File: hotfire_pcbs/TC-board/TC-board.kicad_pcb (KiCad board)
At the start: 2 copper layers, 20.3 x 8.4 mm, 14 parts, among them J1 JST, J2 JST, J3 PCIE-LP-01-01-F-DV-A-TR, U1 MAX31856_Breakout, U2 MAX31856_Breakout

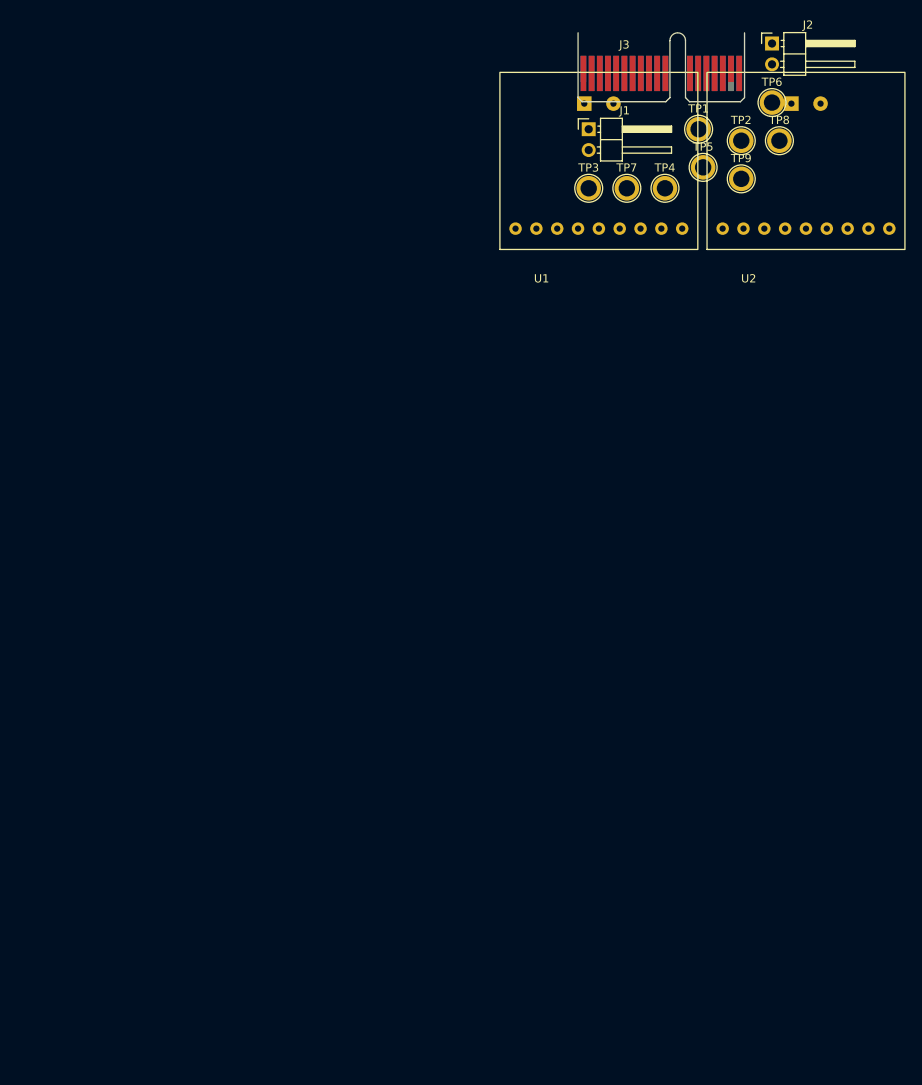
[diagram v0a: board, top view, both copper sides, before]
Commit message: TC Board Layout
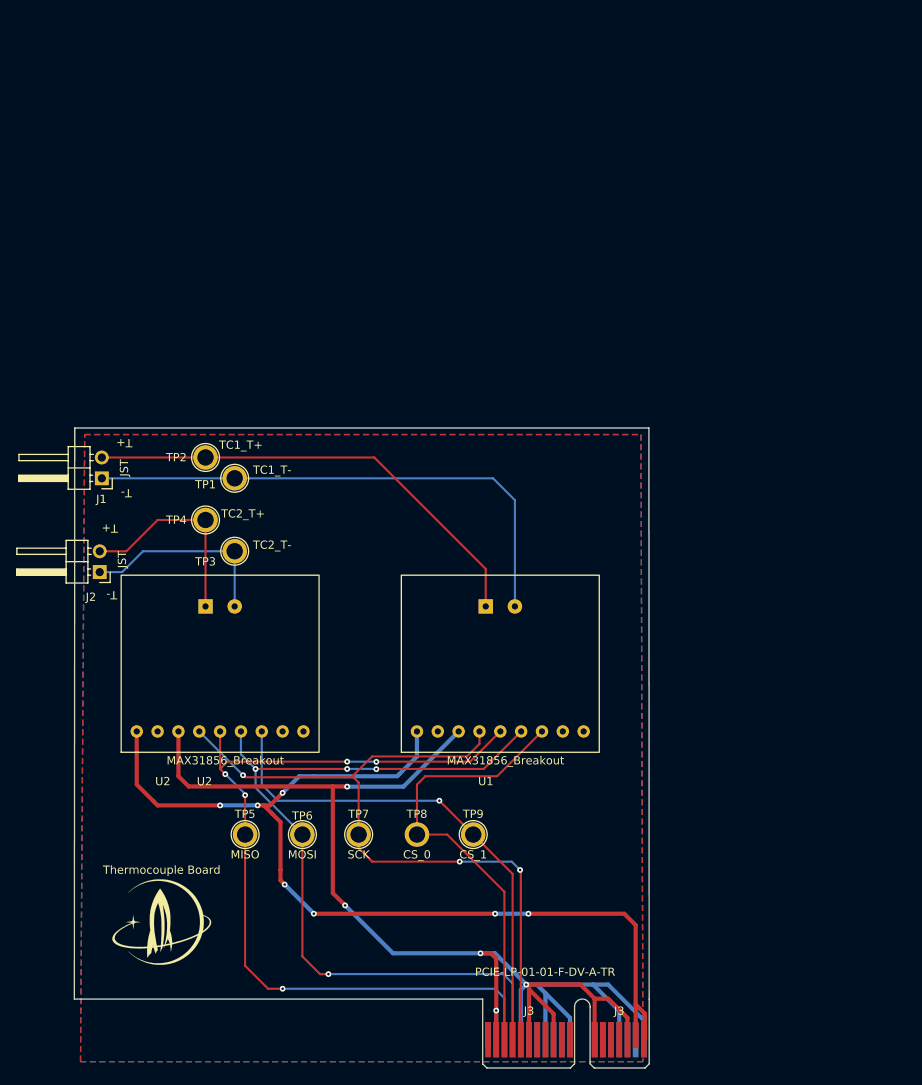
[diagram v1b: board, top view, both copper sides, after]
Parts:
- added G***: LOGO, star-common-lib:star_12x10, F.Cu at (175.8, 120.1)
- added G***: LOGO, LOGO, B.Cu at (227.1, 69.8)
- TP1: value TestPoint -> TC1_T-
- TP2: value TestPoint -> TC1_T+
- TP3: value TestPoint -> TC2_T-
- TP4: value TestPoint -> TC2_T+
- TP5: value TestPoint -> MISO
- TP6: value TestPoint -> MOSI
- TP7: value TestPoint -> SCK
- TP8: value TestPoint -> CS_0; moved to B.Cu
- TP9: value TestPoint -> CS_1
- moved J3 118.4 mm to (215.5, 134.5)
- moved TP6 106.0 mm to (192.9, 109.5)
- moved J2 104.3 mm to (168.2, 77.5), turned to 180 degrees
- moved TP5 98.7 mm to (185.9, 109.5)
- moved TP8 95.4 mm to (206.9, 109.5), turned to 180 degrees
- moved U2 94.1 mm to (183.5, 85.2)
- moved TP9 86.4 mm to (213.7, 109.5)
- moved TP7 85.3 mm to (199.8, 109.5)
- moved TP2 75.9 mm to (181.1, 63.5), turned to 90 degrees
- moved J1 73.0 mm to (168.5, 66.0), turned to 180 degrees
- moved TP1 70.8 mm to (184.7, 66.0), turned to 90 degrees
- moved TP4 69.1 mm to (181.1, 71.1), turned to 90 degrees
- moved U1 62.5 mm to (217.7, 85.2)
- moved TP3 61.8 mm to (184.7, 74.9), turned to 90 degrees
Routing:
- net GND: track 0.00 -> 183.3 mm, vias 0 -> 5
- net +3V3: track 0.00 -> 121.0 mm, vias 0 -> 7
- net /SPI_MISO: track 0.00 -> 104.1 mm, vias 0 -> 5
- net /SPI_MOSI: track 0.00 -> 98.7 mm, vias 0 -> 4
- net /SPI_SCK: track 0.00 -> 90.2 mm, vias 0 -> 3
- net /TC1_T-: track 0.00 -> 64.4 mm
- net /SPI_CS_1: track 0.00 -> 61.8 mm, vias 0 -> 1
- net /TC1_T+: track 0.00 -> 57.0 mm
- net /SPI_CS_0: track 0.00 -> 55.6 mm
- net /TC2_T+: track 0.00 -> 25.0 mm
- net /TC2_T-: track 0.00 -> 24.2 mm
- added copper zone on B.Cu, net GND
- added copper zone on F.Cu, net GND
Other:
- board size 20.3 x 8.4 mm -> 70.1 x 69.6 mm
- board text added: "T+"
- board text added: "T-"
- board text added: "Thermocouple Board"

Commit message: Changed JST to DSUB
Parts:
- removed J2: JST, Connector_PinHeader_2.54mm:PinHeader_1x02_P2.54mm_Horizontal
- J1: value JST -> DB15_Female; footprint Connector_PinHeader_2.54mm:PinHeader_1x02_P2.54mm_Horizontal -> DSUB_622-015-260-042:DSUB_622-015-260-042
- TP1: value TC1_T- -> TestPoint; footprint TestPoint:TestPoint_Plated_Hole_D2.0mm -> TestPoint:TestPoint_Keystone_5010-5014_Multipurpose
- TP2: value TC1_T+ -> TestPoint; footprint TestPoint:TestPoint_Plated_Hole_D2.0mm -> TestPoint:TestPoint_Keystone_5010-5014_Multipurpose
- TP3: value TC2_T- -> TestPoint; footprint TestPoint:TestPoint_Plated_Hole_D2.0mm -> TestPoint:TestPoint_Keystone_5010-5014_Multipurpose
- TP4: value TC2_T+ -> TestPoint; footprint TestPoint:TestPoint_Plated_Hole_D2.0mm -> TestPoint:TestPoint_Keystone_5010-5014_Multipurpose
- TP5: value MISO -> TestPoint; footprint TestPoint:TestPoint_Plated_Hole_D2.0mm -> TestPoint:TestPoint_Keystone_5010-5014_Multipurpose
- TP6: value MOSI -> TestPoint; footprint TestPoint:TestPoint_Plated_Hole_D2.0mm -> TestPoint:TestPoint_Keystone_5010-5014_Multipurpose
- TP7: value SCK -> TestPoint; footprint TestPoint:TestPoint_Plated_Hole_D2.0mm -> TestPoint:TestPoint_Keystone_5010-5014_Multipurpose
- TP8: value CS_0 -> TestPoint; footprint TestPoint:TestPoint_Plated_Hole_D2.0mm -> TestPoint:TestPoint_Keystone_5010-5014_Multipurpose
- TP9: value CS_1 -> TestPoint; footprint TestPoint:TestPoint_Plated_Hole_D2.0mm -> TestPoint:TestPoint_Keystone_5010-5014_Multipurpose
- moved J1 26.7 mm to (176.5, 91.5), turned to -90 degrees
- moved G*** 0.96 mm to (175.8, 121.1)
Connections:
- J1 pad 2: /TC1_T+ -> /TC2_T-
- J3 pad B17: +3V3 -> (no net)
- J3 pad B18: +3V3 -> (no net)
- U1 pad 11: +3V3 -> +3.3V
- U2 pad 11: +3V3 -> +3.3V
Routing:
- net +3V3: track 121.0 -> 0.00 mm, vias 7 -> 0
- net +3.3V: track 0.00 -> 121.0 mm, vias 0 -> 7
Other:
- board text removed: "T+"
- board text removed: "T-"

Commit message: Updated TC Board
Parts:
- TP1: value TestPoint -> TC1_T-
- TP2: value TestPoint -> TC1_T+
- TP3: value TestPoint -> TC2_T-
- TP4: value TestPoint -> TC2_T+
- TP5: value TestPoint -> MISO
- TP6: value TestPoint -> MOSI
- TP7: value TestPoint -> SCK
- TP8: value TestPoint -> CS_0
- TP9: value TestPoint -> CS_1
- moved TP1 39.9 mm to (222.2, 79.5), turned to 0 degrees
- moved TP2 39.1 mm to (216.8, 79.4), turned to 0 degrees
- moved TP5 21.0 mm to (203.3, 121.2)
- moved TP6 21.0 mm to (210.3, 121.2)
- moved TP7 21.0 mm to (217.2, 121.2)
- moved TP8 21.0 mm to (224.3, 121.2)
- moved TP9 21.0 mm to (231.1, 121.2)
- moved U2 13.1 mm to (195.1, 91.4)
- moved TP4 12.8 mm to (190.9, 79.4), turned to 0 degrees
- moved TP3 12.3 mm to (196.1, 79.4), turned to 0 degrees
- moved U1 7.17 mm to (221.2, 91.4)
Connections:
- J3 pad A18: GND -> (no net)
- J3 pad B17: (no net) -> +3.3V
- J3 pad B18: (no net) -> +3.3V
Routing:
- net +3.3V: track 121.0 -> 85.4 mm, vias 7 -> 3
- net /SPI_MOSI: track 98.7 -> 76.2 mm, vias 4 -> 1
- net /SPI_MISO: track 104.1 -> 81.7 mm, vias 5 -> 1
- net /SPI_CS_0: track 55.6 -> 36.8 mm, vias 0 -> 1
- net /SPI_SCK: track 90.2 -> 73.9 mm, vias 3 -> 4
- net /TC2_T-: track 24.2 -> 37.6 mm, vias 0 -> 2
- net /SPI_CS_1: track 61.8 -> 72.0 mm, vias 1 -> 6
- net /TC1_T+: track 57.0 -> 66.2 mm, vias 0 -> 2
- net GND: track 183.3 -> 174.8 mm, vias 5 -> 3
- net /TC2_T+: track 25.0 -> 31.8 mm
- net /TC1_T-: track 64.4 -> 69.3 mm, vias 0 -> 2

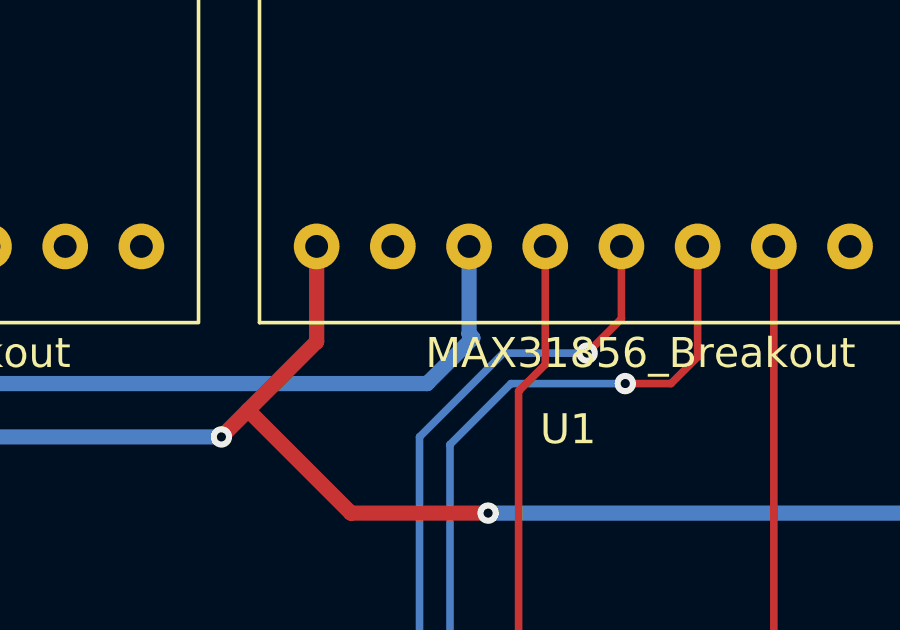
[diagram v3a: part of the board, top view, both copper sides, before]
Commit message: Updated TC Board Layout (as of March 19th)
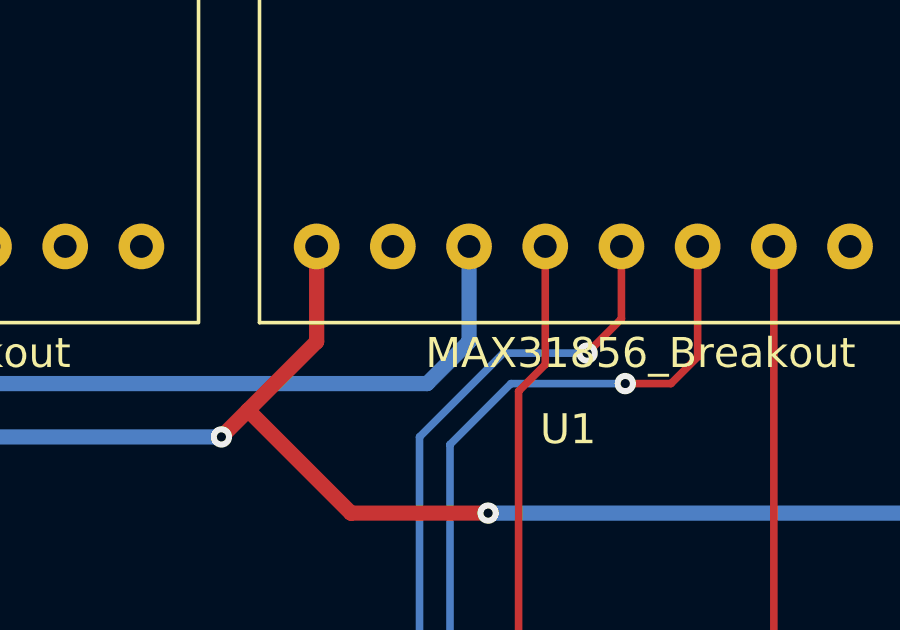
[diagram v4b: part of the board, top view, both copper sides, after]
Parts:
- TP1: value TC1_T- -> TestPoint
- TP2: value TC1_T+ -> TestPoint
- TP3: value TC2_T- -> TestPoint
- TP4: value TC2_T+ -> TestPoint
- TP5: value MISO -> TestPoint
- TP6: value MOSI -> TestPoint
- TP7: value SCK -> TestPoint
- TP8: value CS_0 -> TestPoint
- TP9: value CS_1 -> TestPoint
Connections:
- J3 pad A18: (no net) -> unconnected-(J3-PadA18)
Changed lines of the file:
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@@
   (net 45 "unconnected-(J3-PadA10)")
   (net 46 "unconnected-(J3-PadA1)")
+  (net 47 "unconnected-(J3-PadA18)")
   (footprint "TestPoint:TestPoint_Keystone_5010-5014_Multipurpose" (layer "F.Cu")
     (at 216.789 79.375)
@@
       (effects (font (size 1 1) (thickness 0.15)))
     )
-    (fp_text value "TC1_T+" (at -0.889 2.75) (layer "F.Fab")
+    (fp_text value "TestPoint" (at -0.889 2.75) (layer "F.Fab")
       (effects (font (size 1 1) (thickness 0.15)))
     )
@@
       (effects (font (size 1 1) (thickness 0.15)))
     )
-    (fp_text value "MOSI" (at 0 2.75) (layer "F.Fab")
+    (fp_text value "TestPoint" (at 0 2.75) (layer "F.Fab")
       (effects (font (size 1 1) (thickness 0.15)))
     )
@@
       (effects (font (size 1 1) (thickness 0.15)))
     )
-    (fp_text value "TC2_T+" (at -0.635 2.75) (layer "F.Fab")
+    (fp_text value "TestPoint" (at -0.635 2.75) (layer "F.Fab")
       (effects (font (size 1 1) (thickness 0.15)))
     )
@@
       (effects (font (size 1 1) (thickness 0.15)))
     )
-    (fp_text value "MISO" (at 0 2.75) (layer "F.Fab")
+    (fp_text value "TestPoint" (at 0 2.75) (layer "F.Fab")
       (effects (font (size 1 1) (thickness 0.15)))
     )
@@
       (effects (font (size 1 1) (thickness 0.15)))
     )
-    (fp_text value "SCK" (at 0 2.75) (layer "F.Fab")
+    (fp_text value "TestPoint" (at 0 2.75) (layer "F.Fab")
       (effects (font (size 1 1) (thickness 0.15)))
     )
@@
       (effects (font (size 1 1) (thickness 0.15)))
     )
-    (fp_text value "CS_1" (at 0 2.75) (layer "F.Fab")
+    (fp_text value "TestPoint" (at 0 2.75) (layer "F.Fab")
       (effects (font (size 1 1) (thickness 0.15)))
     )
@@
       (effects (font (size 1 1) (thickness 0.15)))
     )
-    (fp_text value "TC1_T-" (at 1.27 2.75) (layer "F.Fab")
+    (fp_text value "TestPoint" (at 1.27 2.75) (layer "F.Fab")
       (effects (font (size 1 1) (thickness 0.15)))
     )
@@
       (net 40 "unconnected-(J3-PadA17)") (pinfunction "A17") (pintype "passive+no_connect"))
     (pad "A18" connect rect (at 19 0) (size 0.7 4.3) (layers "B.Cu" "B.Mask")
-      (pinfunction "A18") (pintype "passive"))
+      (net 47 "unconnected-(J3-PadA18)") (pinfunction "A18") (pintype "passive+no_connect"))
     (pad "B1" connect rect (at 0 0) (size 0.7 4.3) (layers "F.Cu" "F.Mask")
       (net 36 "unconnected-(J3-PadB1)") (pinfunction "B1") (pintype "passive+no_connect"))
@@
       (effects (font (size 1 1) (thickness 0.15)))
     )
-    (fp_text value "TC2_T-" (at 1.016 2.75) (layer "F.Fab")
+    (fp_text value "TestPoint" (at 1.016 2.75) (layer "F.Fab")
       (effects (font (size 1 1) (thickness 0.15)))
     )
@@
       (effects (font (size 1 1) (thickness 0.15)))
     )
-    (fp_text value "CS_0" (at 0 -2.75) (layer "F.Fab")
+    (fp_text value "TestPoint" (at 0 -2.75) (layer "F.Fab")
       (effects (font (size 1 1) (thickness 0.15)))
     )
@@
   (via (at 216.544 130.928) (size 0.7112) (drill 0.3048) (layers "F.Cu" "B.Cu") (net 6))
   (via (at 221.742 127.254) (size 0.7112) (drill 0.3048) (layers "F.Cu" "B.Cu") (net 6))
-  (segment (start 215.646 106.172) (end 215.519 106.045) (width 0.508) (layer "B.Cu") (net 6))
   (segment (start 231.544 134.481) (end 231.544 128.674) (width 0.508) (layer "B.Cu") (net 6))
   (segment (start 222.544 134.481) (end 222.544 128.738) (width 0.508) (layer "B.Cu") (net 6))
-  (segment (start 193.929 107.696) (end 214.122 107.696) (width 0.508) (layer "B.Cu") (net 6))
   (segment (start 190.754 107.696) (end 190.754 104.648) (width 0.508) (layer "B.Cu") (net 6))
+  (segment (start 214.122 107.696) (end 215.519 106.299) (width 0.508) (layer "B.Cu") (net 6))
   (segment (start 190.754 104.648) (end 190.8175 104.5845) (width 0.508) (layer "B.Cu") (net 6))
   (segment (start 219.544 131.738) (end 222.544 128.738) (width 0.508) (layer "B.Cu") (net 6))
+  (segment (start 215.519 106.299) (end 215.519 103.124) (width 0.508) (layer "B.Cu") (net 6))
   (segment (start 219.544 134.481) (end 219.544 131.738) (width 0.508) (layer "B.Cu") (net 6))
+  (segment (start 193.929 107.696) (end 214.122 107.696) (width 0.508) (layer "B.Cu") (net 6))
   (segment (start 216.544 134.481) (end 216.544 130.928) (width 0.508) (layer "B.Cu") (net 6))
   (segment (start 224.028 127.254) (end 221.742 127.254) (width 0.508) (layer "B.Cu") (net 6))
   (segment (start 225.544 128.278) (end 226.568 127.254) (width 0.508) (layer "B.Cu") (net 6))
   (segment (start 231.544 128.674) (end 230.124 127.254) (width 0.508) (layer "B.Cu") (net 6))
-  (segment (start 214.122 107.696) (end 215.646 106.172) (width 0.508) (layer "B.Cu") (net 6))
+  (segment (start 190.8175 104.5845) (end 193.929 107.696) (width 0.508) (layer "B.Cu") (net 6))
   (segment (start 222.544 128.738) (end 224.028 127.254) (width 0.508) (layer "B.Cu") (net 6))
   (segment (start 230.124 127.254) (end 226.568 127.254) (width 0.508) (layer "B.Cu") (net 6))
   (segment (start 225.544 134.481) (end 225.544 128.278) (width 0.508) (layer "B.Cu") (net 6))
   (segment (start 226.568 127.254) (end 224.028 127.254) (width 0.508) (layer "B.Cu") (net 6))
-  (segment (start 190.8175 104.5845) (end 193.929 107.696) (width 0.508) (layer "B.Cu") (net 6))
   (segment (start 189.357 103.124) (end 190.8175 104.5845) (width 0.508) (layer "B.Cu") (net 6))
-  (segment (start 215.519 106.045) (end 215.519 103.124) (width 0.508) (layer "B.Cu") (net 6))
   (segment (start 210.439 106.299) (end 210.439 103.124) (width 0.508) (layer "F.Cu") (net 17))
   (segment (start 208.153 108.585) (end 211.582 112.014) (width 0.508) (layer "F.Cu") (net 17))
